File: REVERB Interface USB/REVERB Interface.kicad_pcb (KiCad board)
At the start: 2 copper layers, 90.2 x 95.9 mm, 61 parts, among them J1 RPiZeroW, J2 Iridium, J3 APRS, J4 Antenna, J6 USB_B_Micro, J7 USB, J8 USBPOGO, M1 MountingHole_Pad, M2 MountingHole_Pad, M3 MountingHole_Pad, M4 MountingHole_Pad, M5 PiMount, M6 PiMount, M7 PiMount, M8 PiMount, U1 LSM9DS1BOB, U2 MAX3232, U3 CY7C65213-28PVXI, U4 TXB0104D

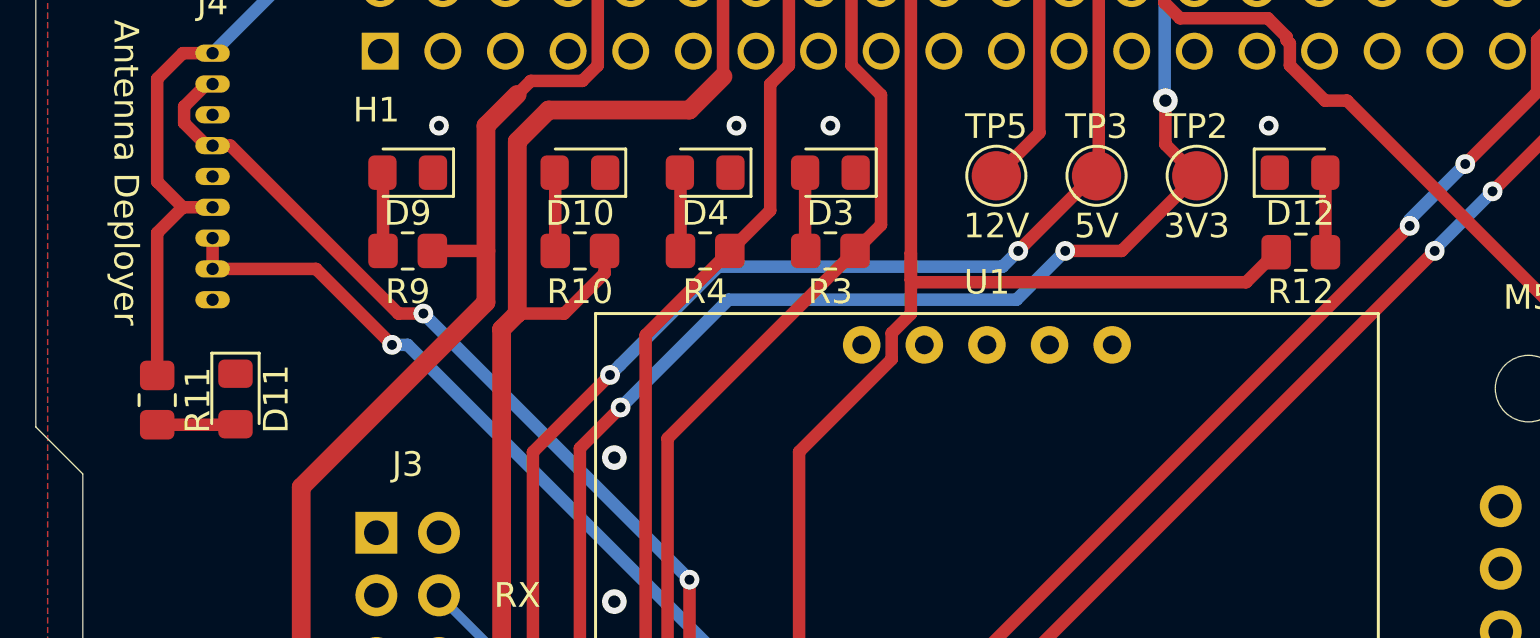
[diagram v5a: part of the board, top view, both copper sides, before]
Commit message: add switch led silkscreen labels
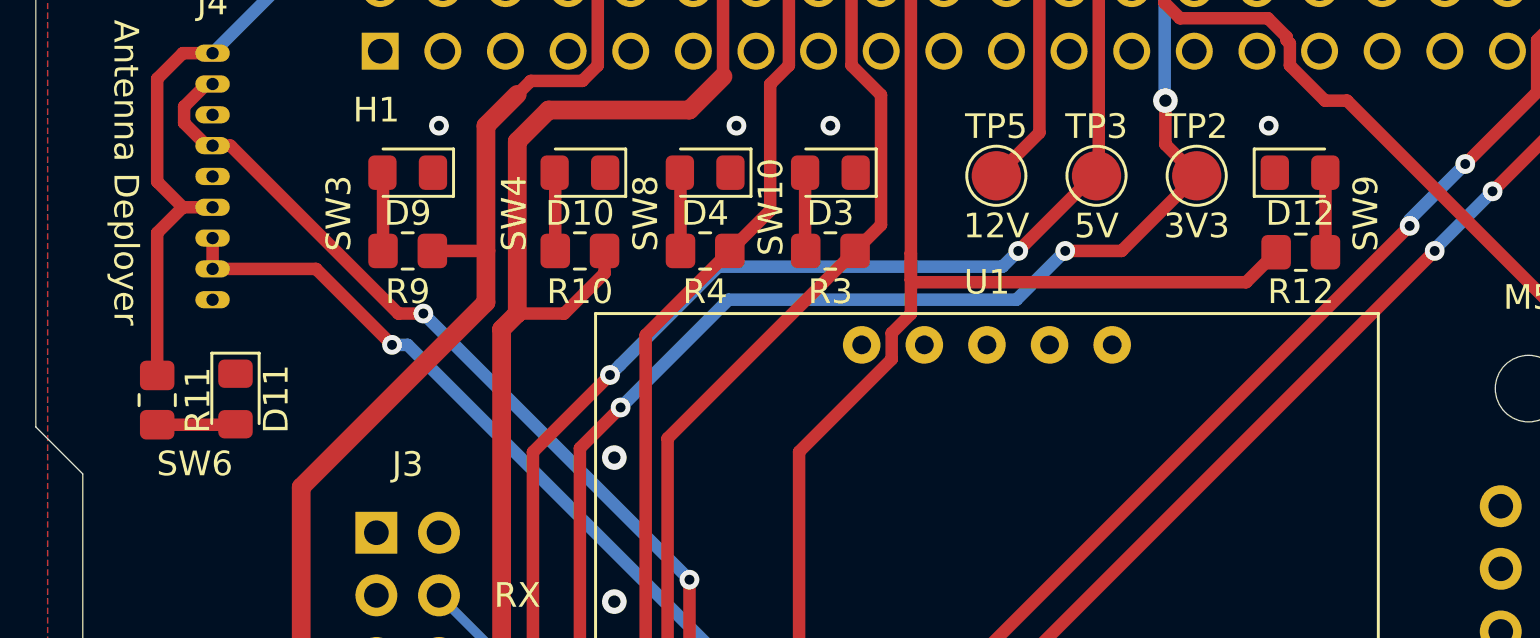
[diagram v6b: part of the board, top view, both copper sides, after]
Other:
- board text added: "SW10"
- board text added: "SW3"
- board text added: "SW4"
- board text added: "SW6"
- board text added: "SW8"
- board text added: "SW9"
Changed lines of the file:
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@@
   (general
     (thickness 1.6)
-    (drawings 66)
+    (drawings 72)
     (tracks 476)
     (zones 0)
@@
   )
   (setup
-    (last_trace_width 0.381)
+    (last_trace_width 0.25)
     (user_trace_width 0.254)
     (user_trace_width 0.381)
@@
     )
   )
+  (gr_text SW6 (at 113.284 82.296) (layer F.SilkS)
+    (effects (font (size 1 1) (thickness 0.15)))
+  )
+  (gr_text SW9 (at 160.782 72.136 90) (layer F.SilkS)
+    (effects (font (size 1 1) (thickness 0.15)))
+  )
+  (gr_text SW10 (at 136.652 71.882 90) (layer F.SilkS)
+    (effects (font (size 1 1) (thickness 0.15)))
+  )
+  (gr_text SW8 (at 131.572 72.136 90) (layer F.SilkS)
+    (effects (font (size 1 1) (thickness 0.15)))
+  )
+  (gr_text SW4 (at 126.238 72.136 90) (layer F.SilkS)
+    (effects (font (size 1 1) (thickness 0.15)))
+  )
+  (gr_text SW3 (at 119.126 72.136 90) (layer F.SilkS)
+    (effects (font (size 1 1) (thickness 0.15)))
+  )
   (gr_text v1.3 (at 195.58 132.715 90) (layer F.SilkS)

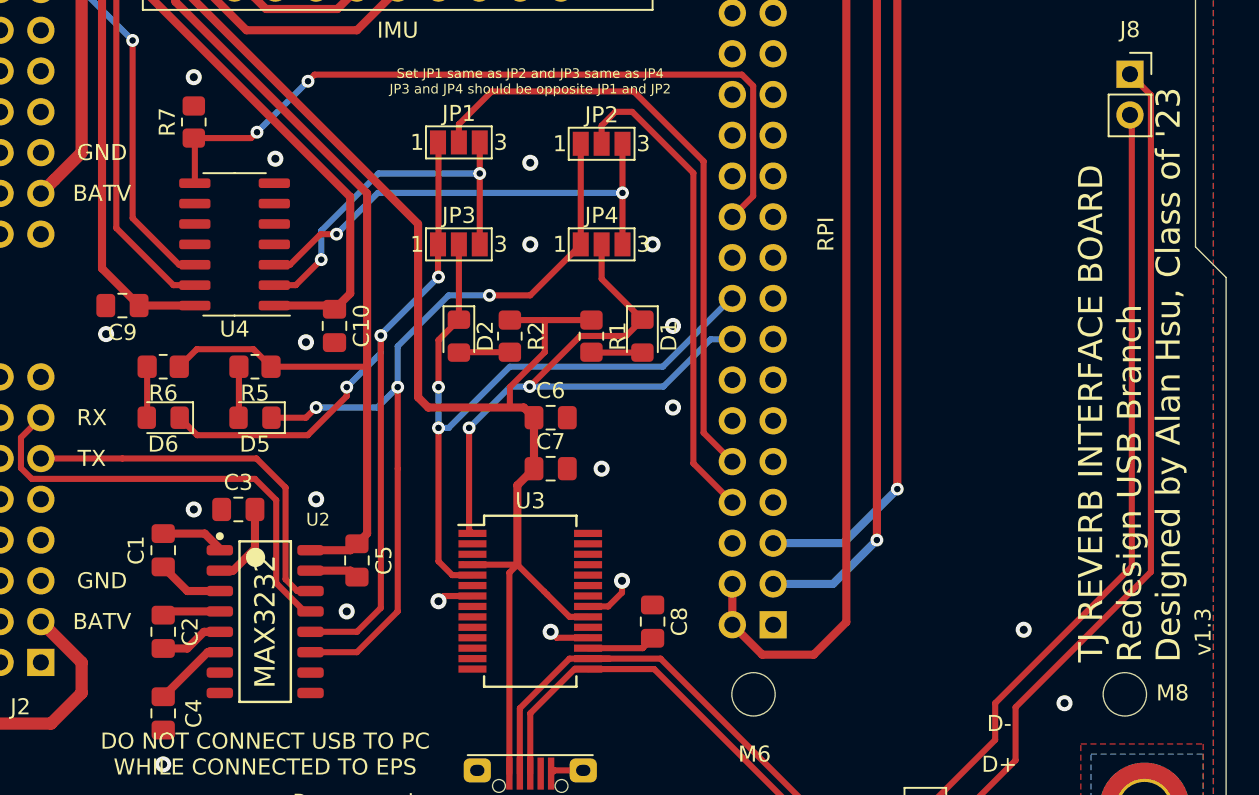
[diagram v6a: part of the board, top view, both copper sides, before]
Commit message: Deprecate SPI branch, push v1.4, add new "multicore" branch, remove combined board files
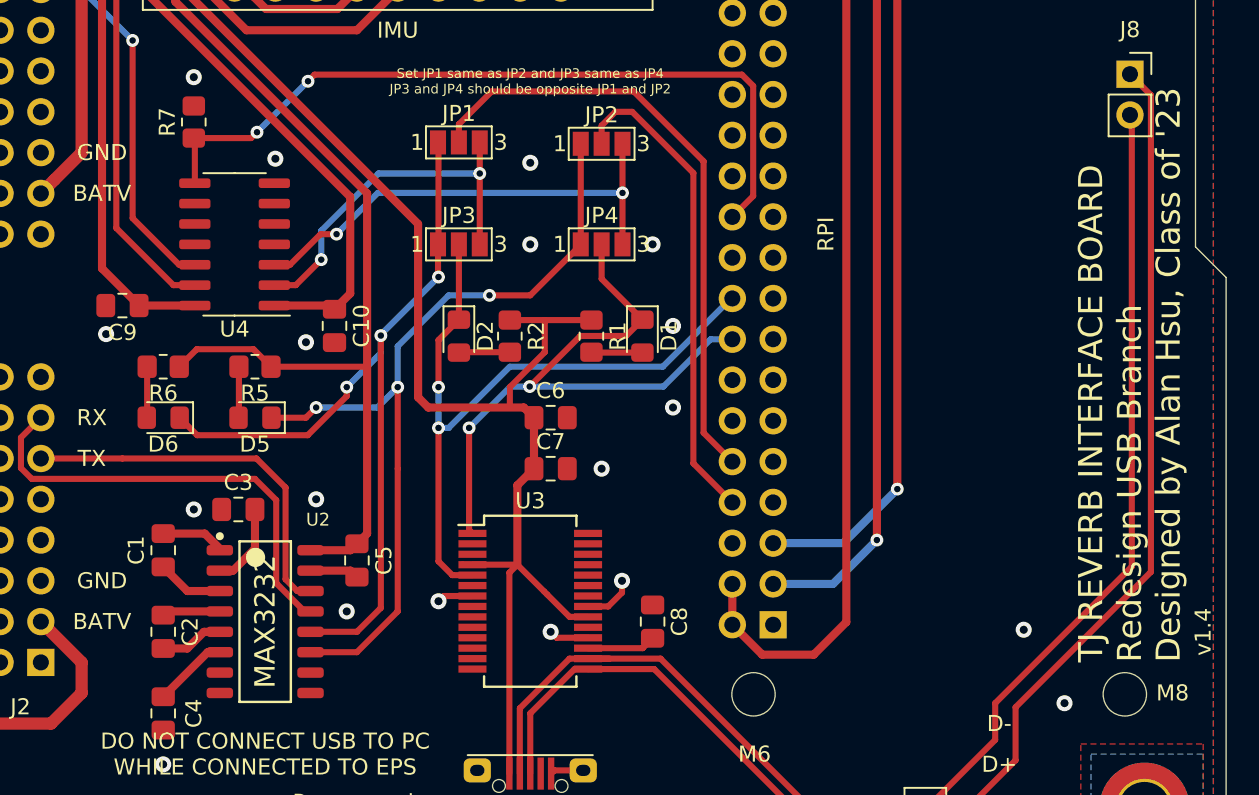
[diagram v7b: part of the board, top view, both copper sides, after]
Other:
- board text added: "v1.4"
- board text removed: "v1.3"
